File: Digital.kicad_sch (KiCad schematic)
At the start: 13 parts, among them J4 I2C_3V3, U5 NLSX4373DR2G, U6 CAT3200-5, U9 QTPY

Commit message: Fix schematic issues (incl QTPY symbol) and some board cleanup
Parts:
- added JP3: MCU_Disable, Jumper:SolderJumper-2_P1.3mm_Bridged_RoundedPad1.0x1.5mm, symbol Jumper:SolderJumper_2_Bridged
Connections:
- net FAULT: now also JP3.1 (A); no longer U9.1 (A0)
- new net: JP3.2 (B), U9.1 (A0)
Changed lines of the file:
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@@
   (junction (at 179.705 92.075) (diameter 0) (color 0 0 0 0)
-  )
-  (junction (at 94.615 40.64) (diameter 0) (color 0 0 0 0)
   )
   (no_connect (at 104.775 65.405))
@@
     (effects (font (size 1.27 1.27)) (justify left bottom))
   )
-  (global_label "FAULT" (shape input) (at 89.535 57.785 180) (fields_autoplaced)
+  (global_label "FAULT" (shape input) (at 81.915 57.785 180) (fields_autoplaced)
     (effects (font (size 1.27 1.27)) (justify right))
-    (property "Intersheetrefs" "${INTERSHEET_REFS}" (at 81.1258 57.785 0)
+    (property "Intersheetrefs" "${INTERSHEET_REFS}" (at 73.5058 57.785 0)
       (effects (font (size 1.27 1.27)) (justify right) hide)
     )
@@
     )
   )
-  (symbol (lib_id "power:PWR_FLAG") (at 84.455 84.455 0) (unit 1)
-    (in_bom yes) (on_board yes) (dnp no) (fields_autoplaced)
-    (property "Reference" "#FLG06" (at 84.455 82.55 0)
-      (effects (font (size 1.27 1.27)) hide)
-    )
-    (property "Value" "PWR_FLAG" (at 84.455 80.645 0)
-      (effects (font (size 1.27 1.27)))
-    )
-    (property "Footprint" "" (at 84.455 84.455 0)
-      (effects (font (size 1.27 1.27)) hide)
-    )
-    (property "Datasheet" "~" (at 84.455 84.455 0)
-      (effects (font (size 1.27 1.27)) hide)
-    )
-    (pin "1")
-    (instances
-      (project "AMF-Generator"
-        (path "/c3df021c-646c-4a68-ac14-a081c2121d02/deb1fbb3-49ca-4dbd-9206-e1712cc02a38"
-          (reference "#FLG06") (unit 1)
-        )
-      )
-    )
-  )
   (symbol (lib_id "power:+3V3") (at 91.44 104.14 180) (unit 1)
     (in_bom yes) (on_board yes) (dnp no)
@@
     )
   )
-  (symbol (lib_id "power:PWR_FLAG") (at 74.93 41.275 0) (unit 1)
-    (in_bom yes) (on_board yes) (dnp no) (fields_autoplaced)
-    (property "Reference" "#FLG07" (at 74.93 39.37 0)
-      (effects (font (size 1.27 1.27)) hide)
-    )
-    (property "Value" "PWR_FLAG" (at 74.93 38.1 0)
-      (effects (font (size 1.27 1.27)))
-    )
-    (property "Footprint" "" (at 74.93 41.275 0)
-      (effects (font (size 1.27 1.27)) hide)
-    )
-    (property "Datasheet" "~" (at 74.93 41.275 0)
-      (effects (font (size 1.27 1.27)) hide)
-    )
-    (pin "1")
-    (instances
-      (project "AMF-Generator"
-        (path "/c3df021c-646c-4a68-ac14-a081c2121d02/deb1fbb3-49ca-4dbd-9206-e1712cc02a38"
-          (reference "#FLG07") (unit 1)
-        )
-      )
-    )
-  )
   (symbol (lib_id "Device:C_Small") (at 160.02 57.15 0) (unit 1)
     (in_bom yes) (on_board yes) (dnp no) (fields_autoplaced)
@@
         (path "/c3df021c-646c-4a68-ac14-a081c2121d02/deb1fbb3-49ca-4dbd-9206-e1712cc02a38"
           (reference "#PWR073") (unit 1)
-        )
-      )
-    )
-  )
-  (symbol (lib_id "power:GND") (at 84.455 84.455 0) (unit 1)
-    (in_bom yes) (on_board yes) (dnp no) (fields_autoplaced)
-    (property "Reference" "#PWR04" (at 84.455 90.805 0)
-      (effects (font (size 1.27 1.27)) hide)
-    )
-    (property "Value" "GND" (at 84.455 89.535 0)
-      (effects (font (size 1.27 1.27)))
-    )
-    (property "Footprint" "" (at 84.455 84.455 0)
-      (effects (font (size 1.27 1.27)) hide)
-    )
-    (property "Datasheet" "" (at 84.455 84.455 0)
-      (effects (font (size 1.27 1.27)) hide)
-    )
-    (pin "1")
-    (instances
-      (project "AMF-Generator"
-        (path "/c3df021c-646c-4a68-ac14-a081c2121d02"
-          (reference "#PWR04") (unit 1)
-        )
-        (path "/c3df021c-646c-4a68-ac14-a081c2121d02/deb1fbb3-49ca-4dbd-9206-e1712cc02a38"
-          (reference "#PWR064") (unit 1)
         )
       )
@@
     )
   )
-  (symbol (lib_id "power:+3V3") (at 74.93 41.275 180) (unit 1)
-    (in_bom yes) (on_board yes) (dnp no) (fields_autoplaced)
-    (property "Reference" "#PWR018" (at 74.93 37.465 0)
-      (effects (font (size 1.27 1.27)) hide)
-    )
-    (property "Value" "+3V3" (at 74.93 45.72 0)
-      (effects (font (size 1.27 1.27)))
-    )
-    (property "Footprint" "" (at 74.93 41.275 0)
-      (effects (font (size 1.27 1.27)) hide)
-    )
-    (property "Datasheet" "" (at 74.93 41.275 0)
+  (symbol (lib_id "Device:C_Small") (at 163.195 88.265 0) (unit 1)
+    (in_bom yes) (on_board yes) (dnp no) (fields_autoplaced)
+    (property "Reference" "C23" (at 166.37 87.6363 0)
+      (effects (font (size 1.27 1.27)) (justify left))
+    )
+    (property "Value" "0.1uF" (at 166.37 90.1763 0)
+      (effects (font (size 1.27 1.27)) (justify left))
+    )
+    (property "Footprint" "Capacitor_SMD:C_0805_2012Metric" (at 163.195 88.265 0)
+      (effects (font (size 1.27 1.27)) hide)
+    )
+    (property "Datasheet" "~" (at 163.195 88.265 0)
+      (effects (font (size 1.27 1.27)) hide)
+    )
+    (pin "1")
+    (pin "2")
+    (instances
+      (project "AMF-Generator"
+        (path "/c3df021c-646c-4a68-ac14-a081c2121d02/deb1fbb3-49ca-4dbd-9206-e1712cc02a38"
+          (reference "C23") (unit 1)
+        )
+      )
+    )
+  )
+  (symbol (lib_id "power:+3V3") (at 99.695 47.625 0) (unit 1)
+    (in_bom yes) (on_board yes) (dnp no) (fields_autoplaced)
+    (property "Reference" "#PWR018" (at 99.695 51.435 0)
+      (effects (font (size 1.27 1.27)) hide)
+    )
+    (property "Value" "+3V3" (at 99.695 43.815 0)
+      (effects (font (size 1.27 1.27)))
+    )
+    (property "Footprint" "" (at 99.695 47.625 0)
+      (effects (font (size 1.27 1.27)) hide)
+    )
+    (property "Datasheet" "" (at 99.695 47.625 0)
       (effects (font (size 1.27 1.27)) hide)
     )
@@
         )
         (path "/c3df021c-646c-4a68-ac14-a081c2121d02/deb1fbb3-49ca-4dbd-9206-e1712cc02a38"
-          (reference "#PWR065") (unit 1)
-        )
-      )
-    )
-  )
-  (symbol (lib_id "Device:C_Small") (at 163.195 88.265 0) (unit 1)
-    (in_bom yes) (on_board yes) (dnp no) (fields_autoplaced)
-    (property "Reference" "C23" (at 166.37 87.6363 0)
-      (effects (font (size 1.27 1.27)) (justify left))
-    )
-    (property "Value" "0.1uF" (at 166.37 90.1763 0)
-      (effects (font (size 1.27 1.27)) (justify left))
-    )
-    (property "Footprint" "Capacitor_SMD:C_0805_2012Metric" (at 163.195 88.265 0)
-      (effects (font (size 1.27 1.27)) hide)
-    )
-    (property "Datasheet" "~" (at 163.195 88.265 0)
-      (effects (font (size 1.27 1.27)) hide)
-    )
-    (pin "1")
-    (pin "2")
-    (instances
-      (project "AMF-Generator"
-        (path "/c3df021c-646c-4a68-ac14-a081c2121d02/deb1fbb3-49ca-4dbd-9206-e1712cc02a38"
-          (reference "C23") (unit 1)
-        )
-      )
-    )
-  )
-  (symbol (lib_id "power:+3V3") (at 99.695 47.625 0) (unit 1)
-    (in_bom yes) (on_board yes) (dnp no) (fields_autoplaced)
-    (property "Reference" "#PWR018" (at 99.695 51.435 0)
-      (effects (font (size 1.27 1.27)) hide)
-    )
-    (property "Value" "+3V3" (at 99.695 43.815 0)
-      (effects (font (size 1.27 1.27)))
-    )
-    (property "Footprint" "" (at 99.695 47.625 0)
-      (effects (font (size 1.27 1.27)) hide)
-    )
-    (property "Datasheet" "" (at 99.695 47.625 0)
-      (effects (font (size 1.27 1.27)) hide)
-    )
-    (pin "1")
-    (instances
-      (project "AMF-Generator"
-        (path "/c3df021c-646c-4a68-ac14-a081c2121d02"
           (reference "#PWR018") (unit 1)
-        )
-        (path "/c3df021c-646c-4a68-ac14-a081c2121d02/deb1fbb3-49ca-4dbd-9206-e1712cc02a38"
-          (reference "#PWR018") (unit 1)
-        )
-      )
-    )
-  )
-  (symbol (lib_id "power:PWR_FLAG") (at 94.615 40.64 0) (unit 1)
-    (in_bom yes) (on_board yes) (dnp no) (fields_autoplaced)
-    (property "Reference" "#FLG03" (at 94.615 38.735 0)
-      (effects (font (size 1.27 1.27)) hide)
-    )
-    (property "Value" "PWR_FLAG" (at 94.615 37.465 0)
-      (effects (font (size 1.27 1.27)))
-    )
-    (property "Footprint" "" (at 94.615 40.64 0)
-      (effects (font (size 1.27 1.27)) hide)
-    )
-    (property "Datasheet" "~" (at 94.615 40.64 0)
-      (effects (font (size 1.27 1.27)) hide)
-    )
-    (pin "1")
-    (instances
-      (project "AMF-Generator"
-        (path "/c3df021c-646c-4a68-ac14-a081c2121d02/deb1fbb3-49ca-4dbd-9206-e1712cc02a38"
-          (reference "#FLG03") (unit 1)
         )
       )
@@
         )
       )
+    )
+  )
+  (symbol (lib_id "Jumper:SolderJumper_2_Bridged") (at 85.725 57.785 0) (unit 1)
+    (in_bom yes) (on_board yes) (dnp no)
+    (property "Reference" "JP3" (at 85.725 53.34 0)
+      (effects (font (size 1.27 1.27)))
+    )
+    (property "Value" "MCU_Disable" (at 85.725 55.245 0)
+      (effects (font (size 1.27 1.27)))
+    )
+    (property "Footprint" "Jumper:SolderJumper-2_P1.3mm_Bridged_RoundedPad1.0x1.5mm" (at 85.725 57.785 0)
+      (effects (font (size 1.27 1.27)) hide)
+    )
+    (property "Datasheet" "~" (at 85.725 57.785 0)
+      (effects (font (size 1.27 1.27)) hide)
+    )
+    (pin "1")
+    (pin "2")
+    (instances
+      (project "AMF-Generator"
+        (path "/c3df021c-646c-4a68-ac14-a081c2121d02/deb1fbb3-49ca-4dbd-9206-e1712cc02a38"
+          (reference "JP3") (unit 1)
+        )
+      )

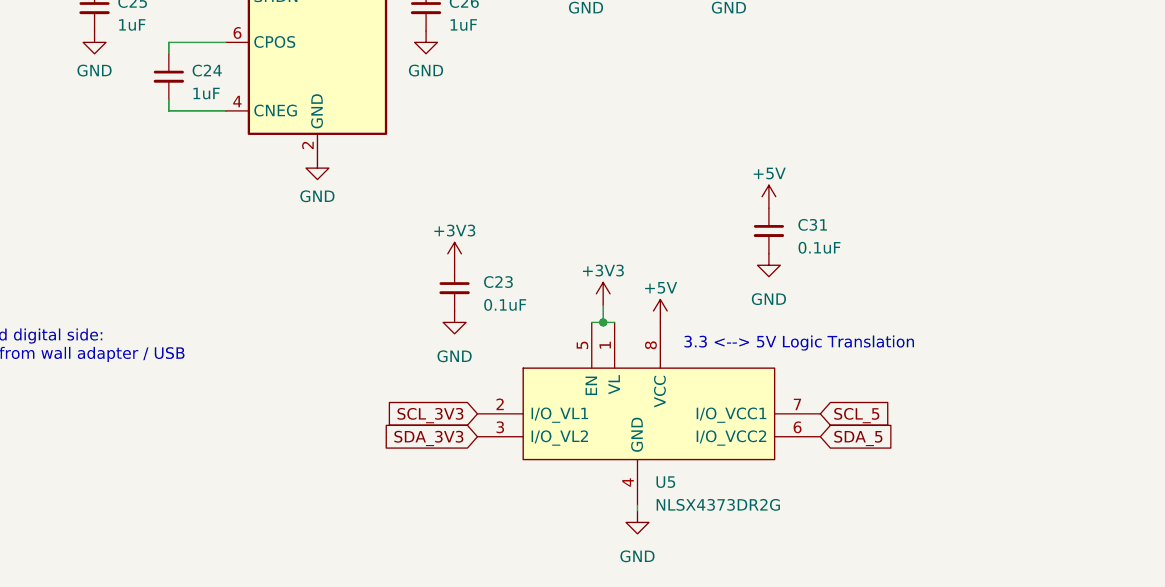
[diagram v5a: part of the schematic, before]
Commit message: Level shifter now obsolete, change to TI part
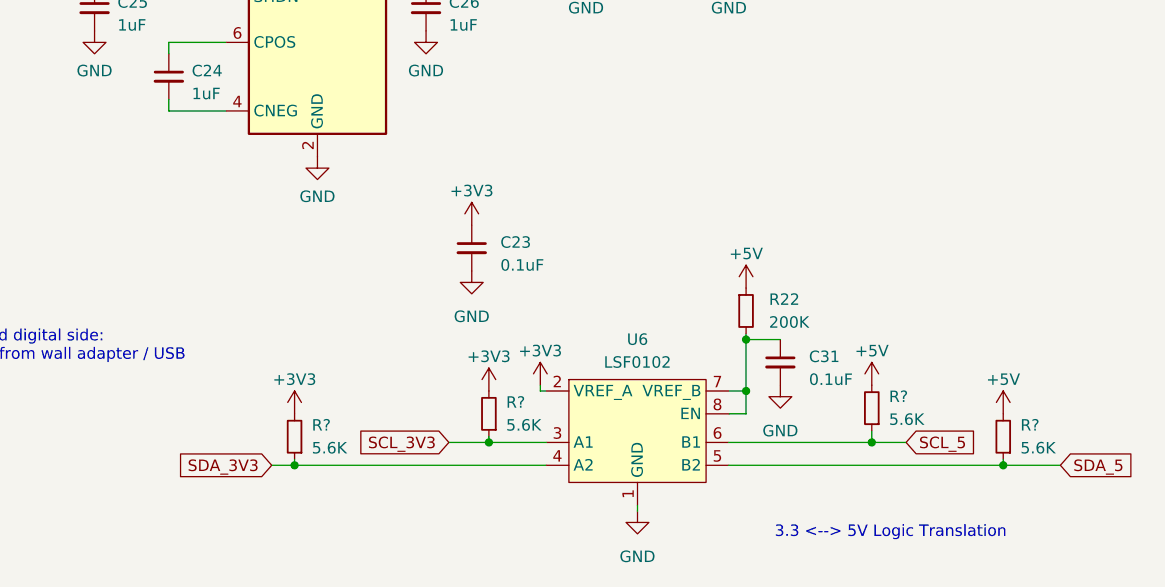
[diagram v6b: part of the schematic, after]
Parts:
- removed U5: NLSX4373DR2G, Package_SO:SOIC-8_3.9x4.9mm_P1.27mm, symbol NLSX4373DR2G:NLSX4373DR2G
- added R22: 200K, Resistor_SMD:R_0805_2012Metric_Pad1.20x1.40mm_HandSolder, symbol Device:R_Small
- added R? (x4): 5.6K, Resistor_SMD:R_0805_2012Metric, symbol Device:R_Small
- added U6: LSF0102, Package_SO:SSOP-8_2.95x2.8mm_P0.65mm, symbol LSF0102:LSF0102
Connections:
- net +3V3: now also R?.2, R?.2, U6.2 (VREF_A)
- net +5V: now also R22.1, R?.2, R?.2; no longer C31.1
- net GND: now also U6.1 (GND)
- net SCL_3V3: now also R?.1, U6.3 (A1)
- net SCL_5: now also R?.1, U6.6 (B1)
- net SDA_3V3: now also R?.1, U6.4 (A2)
- net SDA_5: now also R?.1, U6.5 (B2)
- new net: C31.1, R22.2, U6.7 (VREF_B), U6.8 (EN)
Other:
- moved on the sheet: C23, C31

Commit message: Layout updated. Silk still WIP
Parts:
- removed C23: 0.1uF, Capacitor_SMD:C_0805_2012Metric, symbol Device:C_Small
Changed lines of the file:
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@@
-    )
-  )
-  (symbol (lib_id "power:GND") (at 165.1 86.36 0) (unit 1)
-    (in_bom yes) (on_board yes) (dnp no) (fields_autoplaced)
-    (property "Reference" "#PWR037" (at 165.1 92.71 0)
-      (effects (font (size 1.27 1.27)) hide)
-    )
-    (property "Value" "GND" (at 165.1 91.44 0)
-      (effects (font (size 1.27 1.27)))
-    )
-    (property "Footprint" "" (at 165.1 86.36 0)
-      (effects (font (size 1.27 1.27)) hide)
-    )
-    (property "Datasheet" "" (at 165.1 86.36 0)
-      (effects (font (size 1.27 1.27)) hide)
-    )
-    (pin "1")
-    (instances
-      (project "AMF-Generator"
-        (path "/c3df021c-646c-4a68-ac14-a081c2121d02"
-          (reference "#PWR037") (unit 1)
-        )
-        (path "/c3df021c-646c-4a68-ac14-a081c2121d02/deb1fbb3-49ca-4dbd-9206-e1712cc02a38"
-          (reference "#PWR047") (unit 1)
-        )
-      )
     )
   )
@@
         (path "/c3df021c-646c-4a68-ac14-a081c2121d02/deb1fbb3-49ca-4dbd-9206-e1712cc02a38"
           (reference "C31") (unit 1)
-        )
-      )
-    )
-  )
-  (symbol (lib_id "power:+3V3") (at 165.1 81.28 0) (unit 1)
-    (in_bom yes) (on_board yes) (dnp no) (fields_autoplaced)
-    (property "Reference" "#PWR038" (at 165.1 85.09 0)
-      (effects (font (size 1.27 1.27)) hide)
-    )
-    (property "Value" "+3V3" (at 165.1 77.47 0)
-      (effects (font (size 1.27 1.27)))
-    )
-    (property "Footprint" "" (at 165.1 81.28 0)
-      (effects (font (size 1.27 1.27)) hide)
-    )
-    (property "Datasheet" "" (at 165.1 81.28 0)
-      (effects (font (size 1.27 1.27)) hide)
-    )
-    (pin "1")
-    (instances
-      (project "AMF-Generator"
-        (path "/c3df021c-646c-4a68-ac14-a081c2121d02"
-          (reference "#PWR038") (unit 1)
-        )
-        (path "/c3df021c-646c-4a68-ac14-a081c2121d02/deb1fbb3-49ca-4dbd-9206-e1712cc02a38"
-          (reference "#PWR046") (unit 1)
         )
       )
@@
         )
       )
-    )
-  )
-  (symbol (lib_id "Device:C_Small") (at 165.1 83.82 0) (unit 1)
-    (in_bom yes) (on_board yes) (dnp no) (fields_autoplaced)
-    (property "Reference" "C23" (at 168.275 83.1913 0)
-      (effects (font (size 1.27 1.27)) (justify left))
-    )
-    (property "Value" "0.1uF" (at 168.275 85.7313 0)
-      (effects (font (size 1.27 1.27)) (justify left))
-    )
-    (property "Footprint" "Capacitor_SMD:C_0805_2012Metric" (at 165.1 83.82 0)
-      (effects (font (size 1.27 1.27)) hide)
-    )
-    (property "Datasheet" "~" (at 165.1 83.82 0)
-      (effects (font (size 1.27 1.27)) hide)
-    )
-    (pin "1")
-    (pin "2")
-    (instances
-      (project "AMF-Generator"
-        (path "/c3df021c-646c-4a68-ac14-a081c2121d02/deb1fbb3-49ca-4dbd-9206-e1712cc02a38"
-          (reference "C23") (unit 1)
-        )
-      )
